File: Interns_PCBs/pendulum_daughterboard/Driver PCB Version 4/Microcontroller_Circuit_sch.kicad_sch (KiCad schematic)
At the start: 7 parts, among them J1 AVR-ISP-6, SW1 SW_Push, U10 ATtiny85-20S

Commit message: Another Drive PCB
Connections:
- net 5V renamed 3.3V
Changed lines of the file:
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@@
     (stroke (width 0) (type default) (color 0 0 0 0))
+  )
+  (global_label "3.3V" (shape input) (at 146.05 30.48 90) (fields_autoplaced)
+    (effects (font (size 1.27 1.27)) (justify left))
+    (property "Intersheet References" "${INTERSHEET_REFS}" (id 0) (at 145.9706 23.9545 90)
+      (effects (font (size 1.27 1.27)) (justify left) hide)
+    )
   )
   (hierarchical_label "GND" (shape input) (at 104.14 104.14 90)
@@
     (effects (font (size 1.27 1.27)) (justify left))
   )
-  (hierarchical_label "5V" (shape input) (at 158.75 113.03 0)
+  (hierarchical_label "3.3V" (shape input) (at 158.75 113.03 0)
     (effects (font (size 1.27 1.27)) (justify left))
   )
@@
     (effects (font (size 1.27 1.27)) (justify right))
   )
-  (hierarchical_label "5V" (shape input) (at 146.05 30.48 90)
-    (effects (font (size 1.27 1.27)) (justify left))
-  )
   (symbol (lib_id "MCU_Microchip_ATtiny:ATtiny85-20S") (at 190.5 87.63 0) (mirror y) (unit 1)

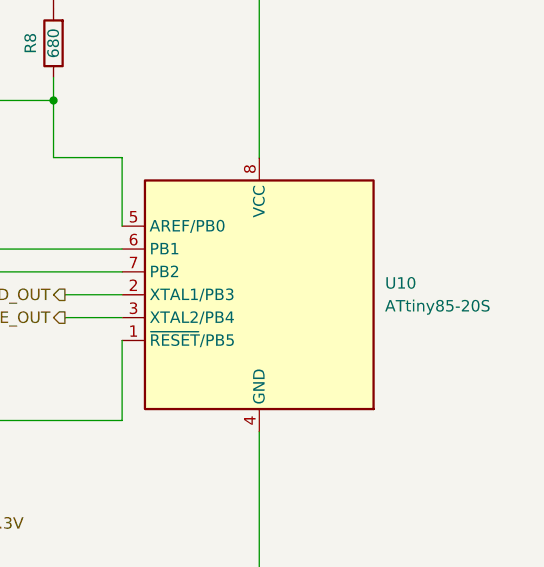
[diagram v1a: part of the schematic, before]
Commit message: 3.3V PCB Design
PCB with 2 voltage regulators, regulating both the 5V input from the digital pins and the external 5V from the terminal block.
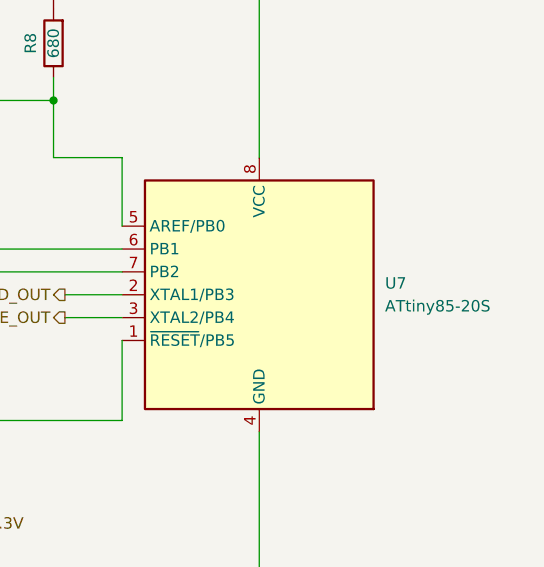
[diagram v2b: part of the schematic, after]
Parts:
- renumbered U10 to U7
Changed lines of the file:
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@@
   (symbol (lib_id "MCU_Microchip_ATtiny:ATtiny85-20S") (at 190.5 87.63 0) (mirror y) (unit 1)
     (in_bom yes) (on_board yes) (fields_autoplaced)
-    (property "Reference" "U10" (id 0) (at 204.47 86.3599 0)
+    (property "Reference" "U7" (id 0) (at 204.47 86.3599 0)
       (effects (font (size 1.27 1.27)) (justify right))
     )
